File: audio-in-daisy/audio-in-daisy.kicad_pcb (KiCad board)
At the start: 2 copper layers, 25 x 19 mm, 13 parts, among them J1 IN, J2 OUT, J3 POWER, U1 TL072

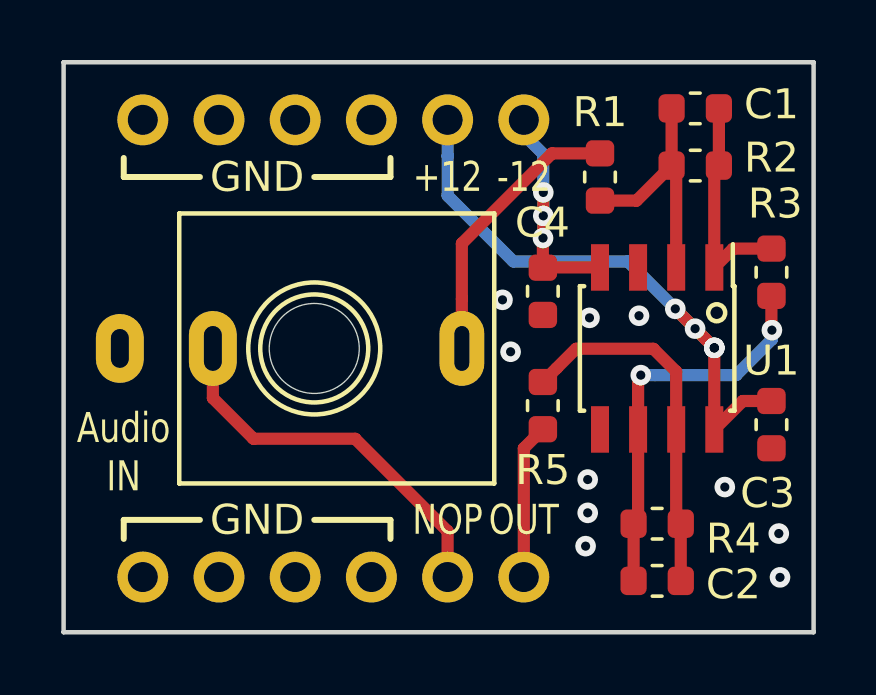
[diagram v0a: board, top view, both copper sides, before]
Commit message: Add audio-in-daisy direct input pin
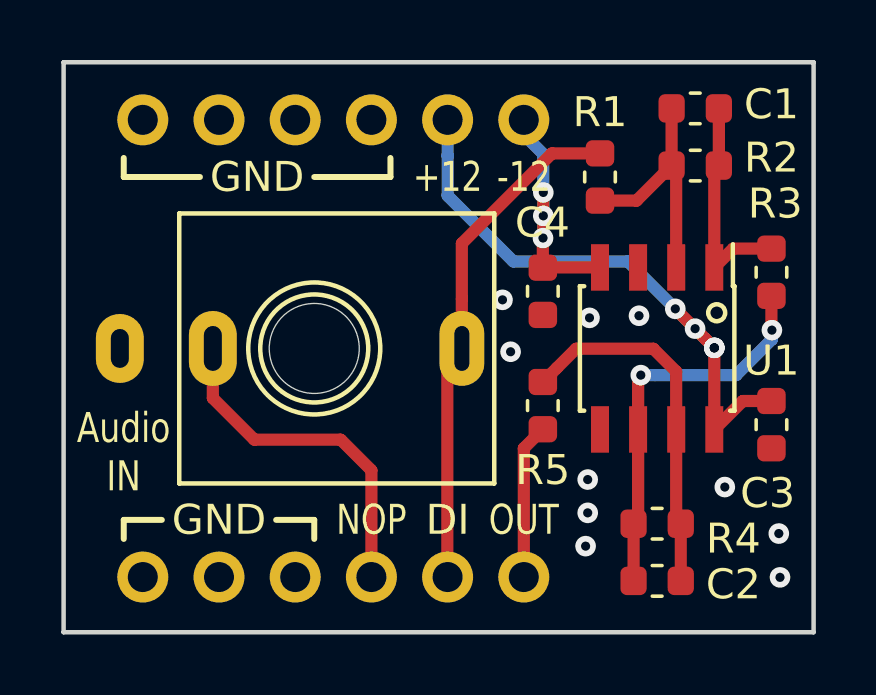
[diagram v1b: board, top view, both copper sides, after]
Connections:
- J1 pad T: Net-(J1-PadT) -> DI
- J2 pad 2: NOP -> DI
- J2 pad 3: GND -> NOP
- R1 pad 2: Net-(J1-PadT) -> DI
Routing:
- net DI: track 0.00 -> 17.2 mm
- net Net-(J1-PadT): track 9.35 -> 0.00 mm
- net NOP: track 12.8 -> 11.5 mm
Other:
- board text added: "DI"
